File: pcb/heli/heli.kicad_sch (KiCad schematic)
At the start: 32 parts, among them J1 Batterie, J2 Debug, J3 Radio, J4 Servo, J5 Servo, Q1 IRLZ44N, SW1 SW_MEC_5E, U1 AZ1117-3.3, U2 MPU-6050, U3 STM32F103CBTx, Y1 8MHz

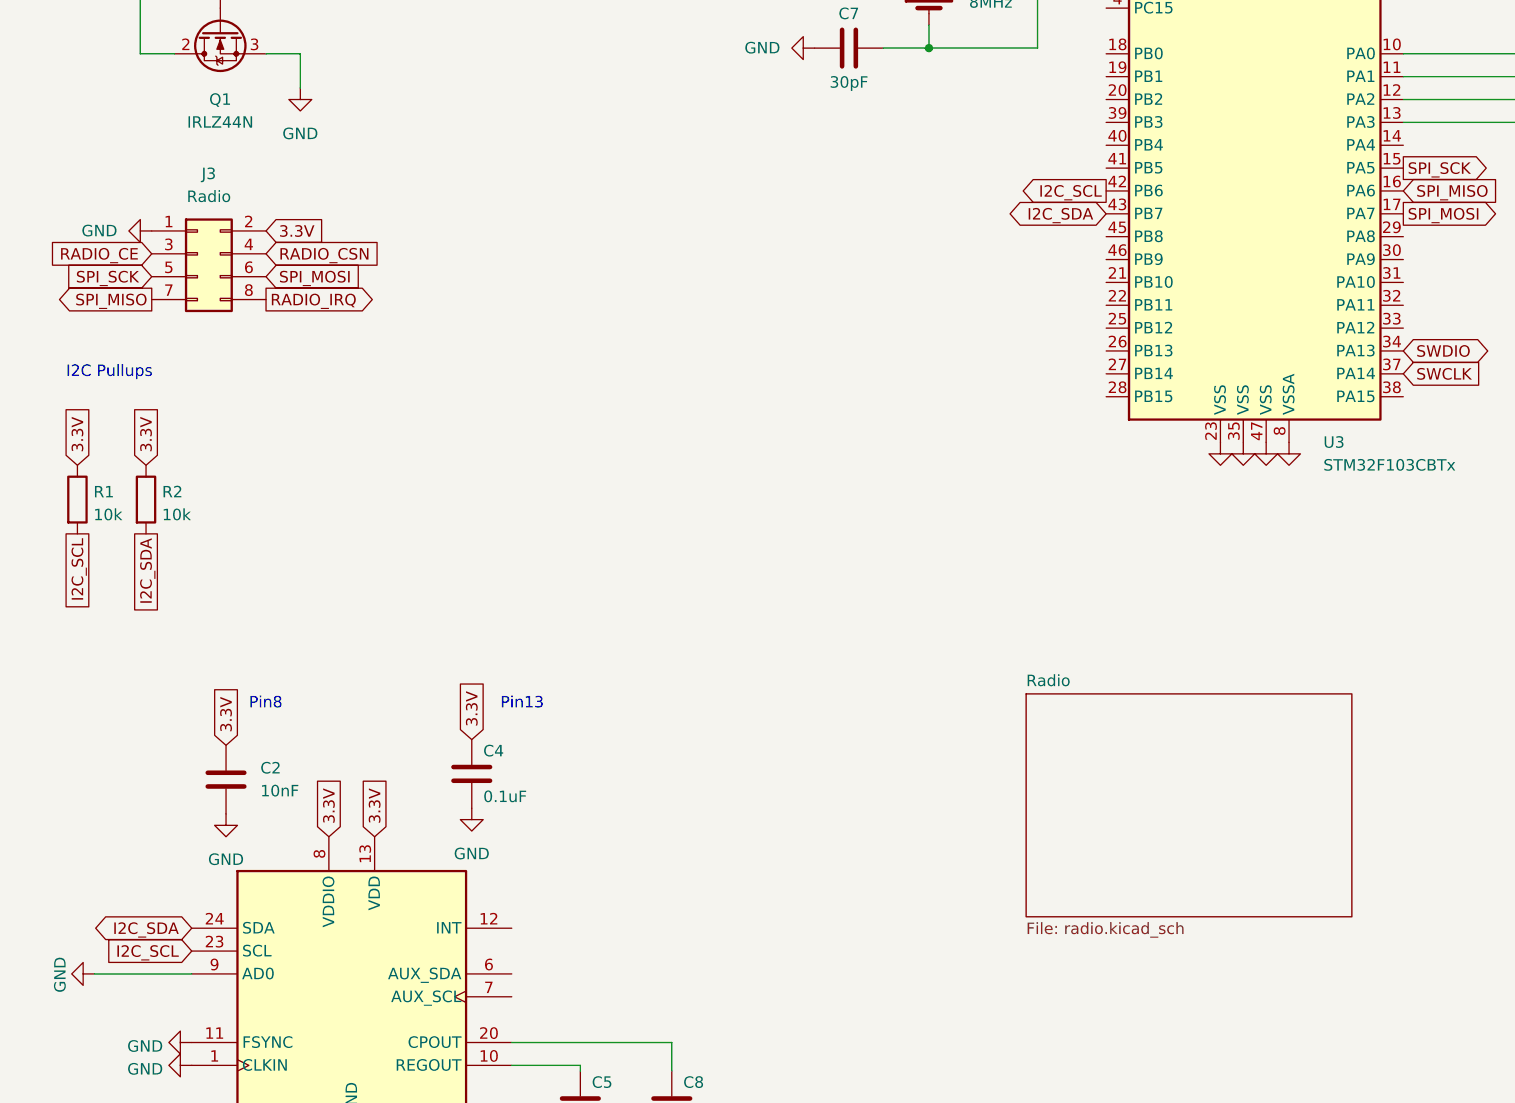
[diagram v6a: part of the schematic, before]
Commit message: 
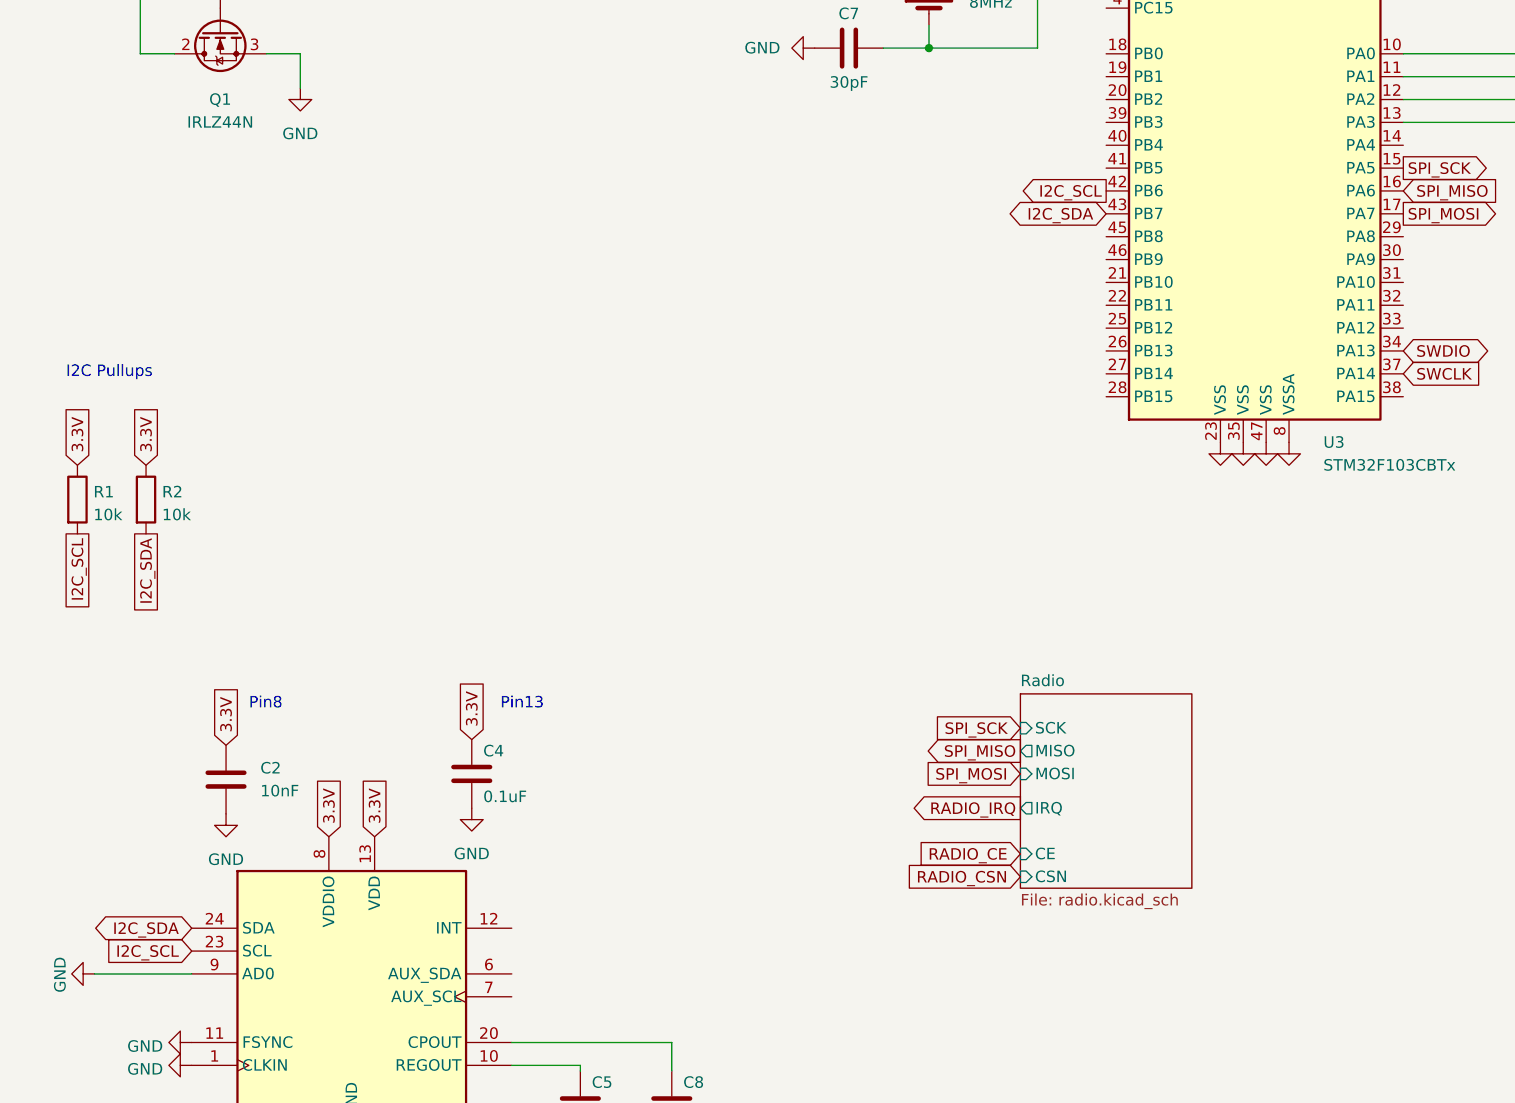
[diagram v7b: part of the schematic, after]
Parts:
- removed J3: Radio, Connector_PinHeader_2.54mm:PinHeader_2x04_P2.54mm_Vertical, symbol Connector_Generic:Conn_02x04_Odd_Even
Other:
- sheet Radio ports: added CE, CSN, IRQ, MISO, MOSI, SCK; removed none

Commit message: 
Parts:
- Y1: footprint Crystal:Crystal_HC49-4H_Vertical -> Crystal:Crystal_SMD_HC49-SD
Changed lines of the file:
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@@
       (effects (font (size 1.27 1.27)) (justify right))
     )
-    (property "Footprint" "Crystal:Crystal_HC49-4H_Vertical" (id 2) (at 116.84 60.325 0)
+    (property "Footprint" "Crystal:Crystal_SMD_HC49-SD" (id 2) (at 116.84 60.325 0)
       (effects (font (size 1.27 1.27)) hide)
     )
@@
       (reference "#PWR0113") (unit 1) (value "GND") (footprint "")
     )
+    (path "/ff163e09-1c9a-4e9f-9fc2-cd2f8ec1c6f1/361a901c-4a32-4ced-b2fe-ab2844887a0a"
+      (reference "#PWR0114") (unit 1) (value "GND") (footprint "")
+    )
+    (path "/ff163e09-1c9a-4e9f-9fc2-cd2f8ec1c6f1/8549edc8-7868-445e-8e60-f5cdb289851b"
+      (reference "#PWR0115") (unit 1) (value "GND") (footprint "")
+    )
+    (path "/ff163e09-1c9a-4e9f-9fc2-cd2f8ec1c6f1/c95310af-53ca-4059-86cc-278f5cf1ab51"
+      (reference "#PWR0116") (unit 1) (value "GND") (footprint "")
+    )
+    (path "/ff163e09-1c9a-4e9f-9fc2-cd2f8ec1c6f1/2487208e-e563-4264-98f5-c6523d50a5c6"
+      (reference "#PWR0117") (unit 1) (value "GND") (footprint "")
+    )
+    (path "/ff163e09-1c9a-4e9f-9fc2-cd2f8ec1c6f1/857ae3b4-3ab8-49f2-ba21-4f6834532cc8"
+      (reference "#PWR0118") (unit 1) (value "GND") (footprint "")
+    )
     (path "/a695f418-bc3a-4046-8cf8-067ebffee1a8"
       (reference "C1") (unit 1) (value "10uF") (footprint "Capacitor_SMD:CP_Elec_4x5.4")
@@
       (reference "C24") (unit 1) (value "1nF") (footprint "Capacitor_SMD:C_0603_1608Metric")
     )
+    (path "/ff163e09-1c9a-4e9f-9fc2-cd2f8ec1c6f1/2efc0c9c-1f91-41ea-81d3-ea526dfa618c"
+      (reference "C25") (unit 1) (value "100nF") (footprint "Capacitor_SMD:C_0603_1608Metric")
+    )
+    (path "/ff163e09-1c9a-4e9f-9fc2-cd2f8ec1c6f1/0950225b-258f-431f-ac35-977d3ffe7815"
+      (reference "C26") (unit 1) (value "100nF") (footprint "Capacitor_SMD:C_0603_1608Metric")
+    )
     (path "/b28a0e5f-aecf-489c-9fc5-7ef0cd88e703"
       (reference "D1") (unit 1) (value "LED") (footprint "LED_SMD:LED_0603_1608Metric")
@@
     )
     (path "/7167ad50-a0fe-4dd3-bd80-1cc072116538"
-      (reference "Y1") (unit 1) (value "8MHz") (footprint "Crystal:Crystal_HC49-4H_Vertical")
+      (reference "Y1") (unit 1) (value "8MHz") (footprint "Crystal:Crystal_SMD_HC49-SD")
     )
     (path "/8972c389-56a6-466a-9271-66b0ec918c0e/20c969fe-611b-4c16-bd51-c9b74f3165f8"
-      (reference "Y2") (unit 1) (value "16MHz") (footprint "Crystal:Crystal_HC49-4H_Vertical")
-    )
-  )
+      (reference "Y2") (unit 1) (value "16MHz") (footprint "Crystal:Crystal_SMD_HC49-SD")
+    )
+  )
